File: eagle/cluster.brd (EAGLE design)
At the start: 24.9 x 28.4 mm, 12 parts, among them J1 B7B-ZR_(LF)(SN)

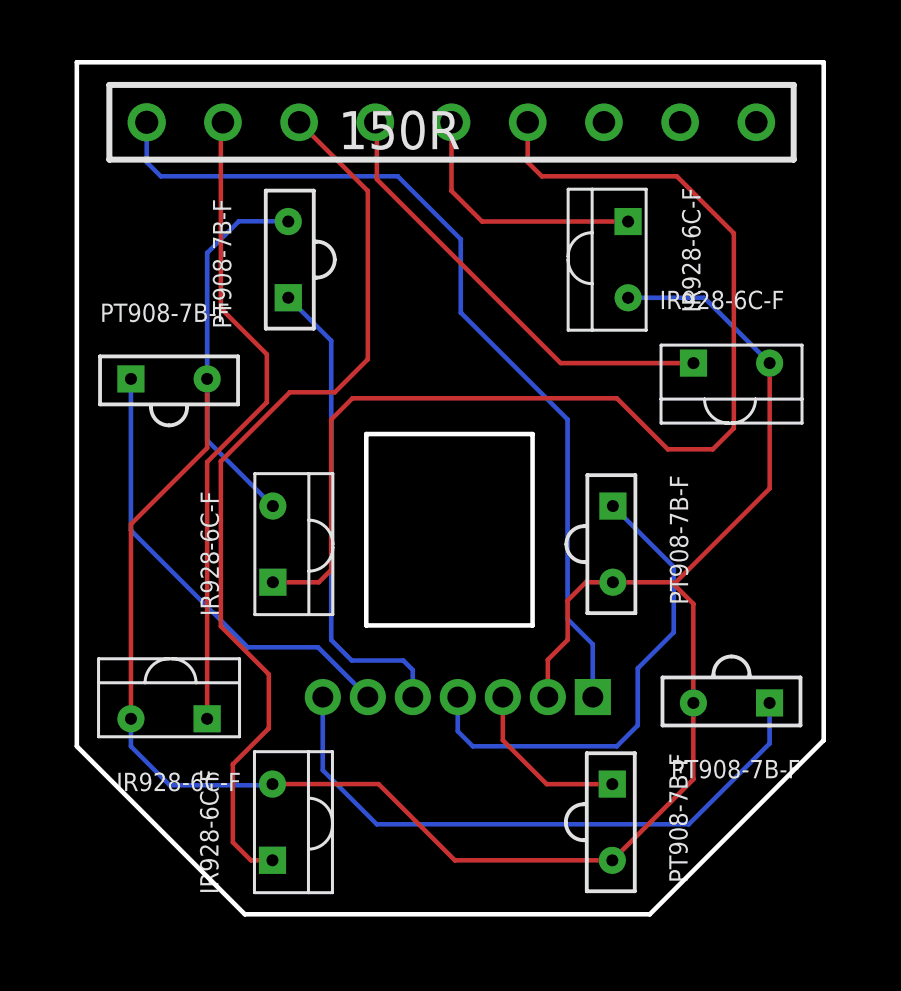
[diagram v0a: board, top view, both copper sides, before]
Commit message: Fix drill holes and outer dimensions on cluster and left thumb cluster
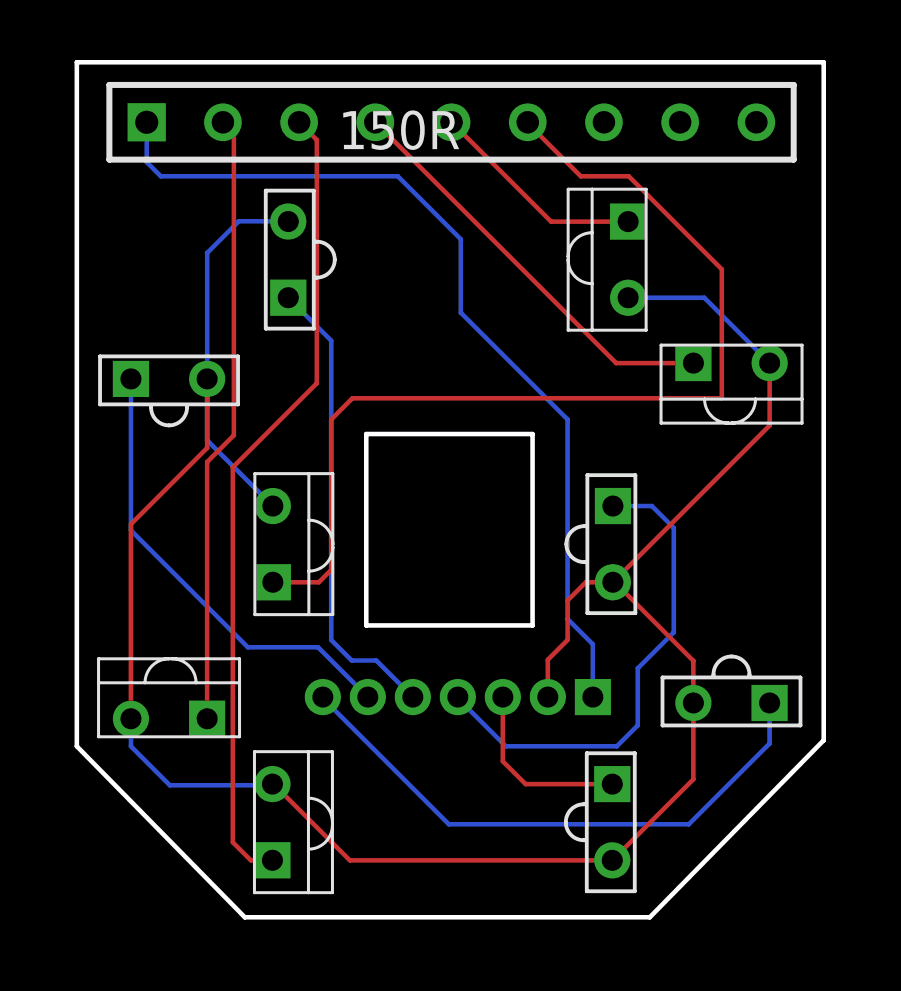
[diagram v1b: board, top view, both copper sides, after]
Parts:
- 150R: value 4309R-101-202LF -> 150R; device 4309R-101-202LF:4309R-101 -> 9 pin resistor network:9PIN-RESISTOR-NETWORK
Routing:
- net N$6: track 37.5 -> 33.3 mm
- net N$3: track 30.6 -> 27.0 mm
- net N$9: track 20.5 -> 19.1 mm
- net N$5: track 8.60 -> 7.26 mm
- net N$4: track 15.0 -> 13.9 mm
- net N$2: track 21.4 -> 20.4 mm
- net N$10: track 16.0 -> 15.5 mm
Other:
- board size 24.9 x 28.4 mm -> 24.9 x 28.5 mm

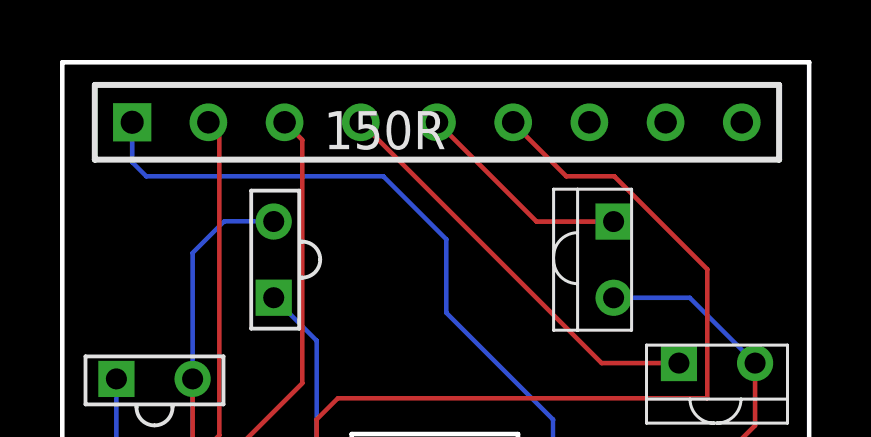
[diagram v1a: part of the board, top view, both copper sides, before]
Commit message: Reduce drill size of resistor holes. Fix right thumb cluster
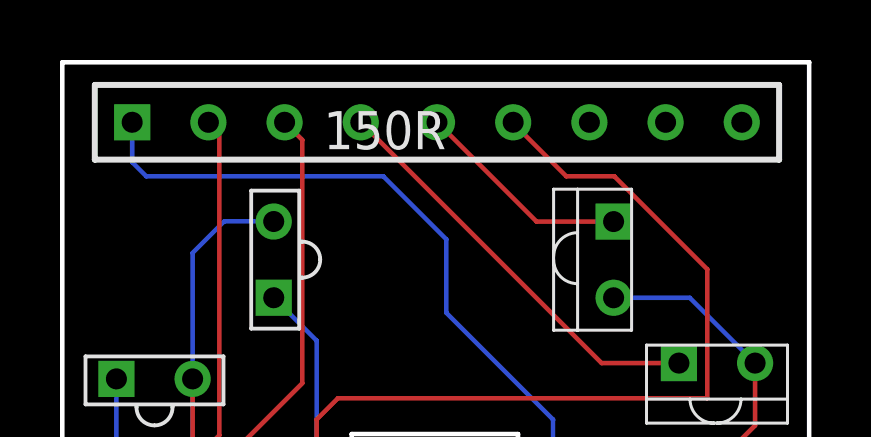
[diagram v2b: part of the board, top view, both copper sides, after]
